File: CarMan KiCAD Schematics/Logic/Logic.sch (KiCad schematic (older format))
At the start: 33 parts, among them J1 MC_CAN, J3 IMU, J4 RTC, J5 Conn to TSI Board, J6 You're Welcome -Ethan, J7 RTC, J8 PIC program, U1 MCP9700AT-HTT, U3 PIC32MZ2048EFM064-I_PT, U5 ISO1050DUB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

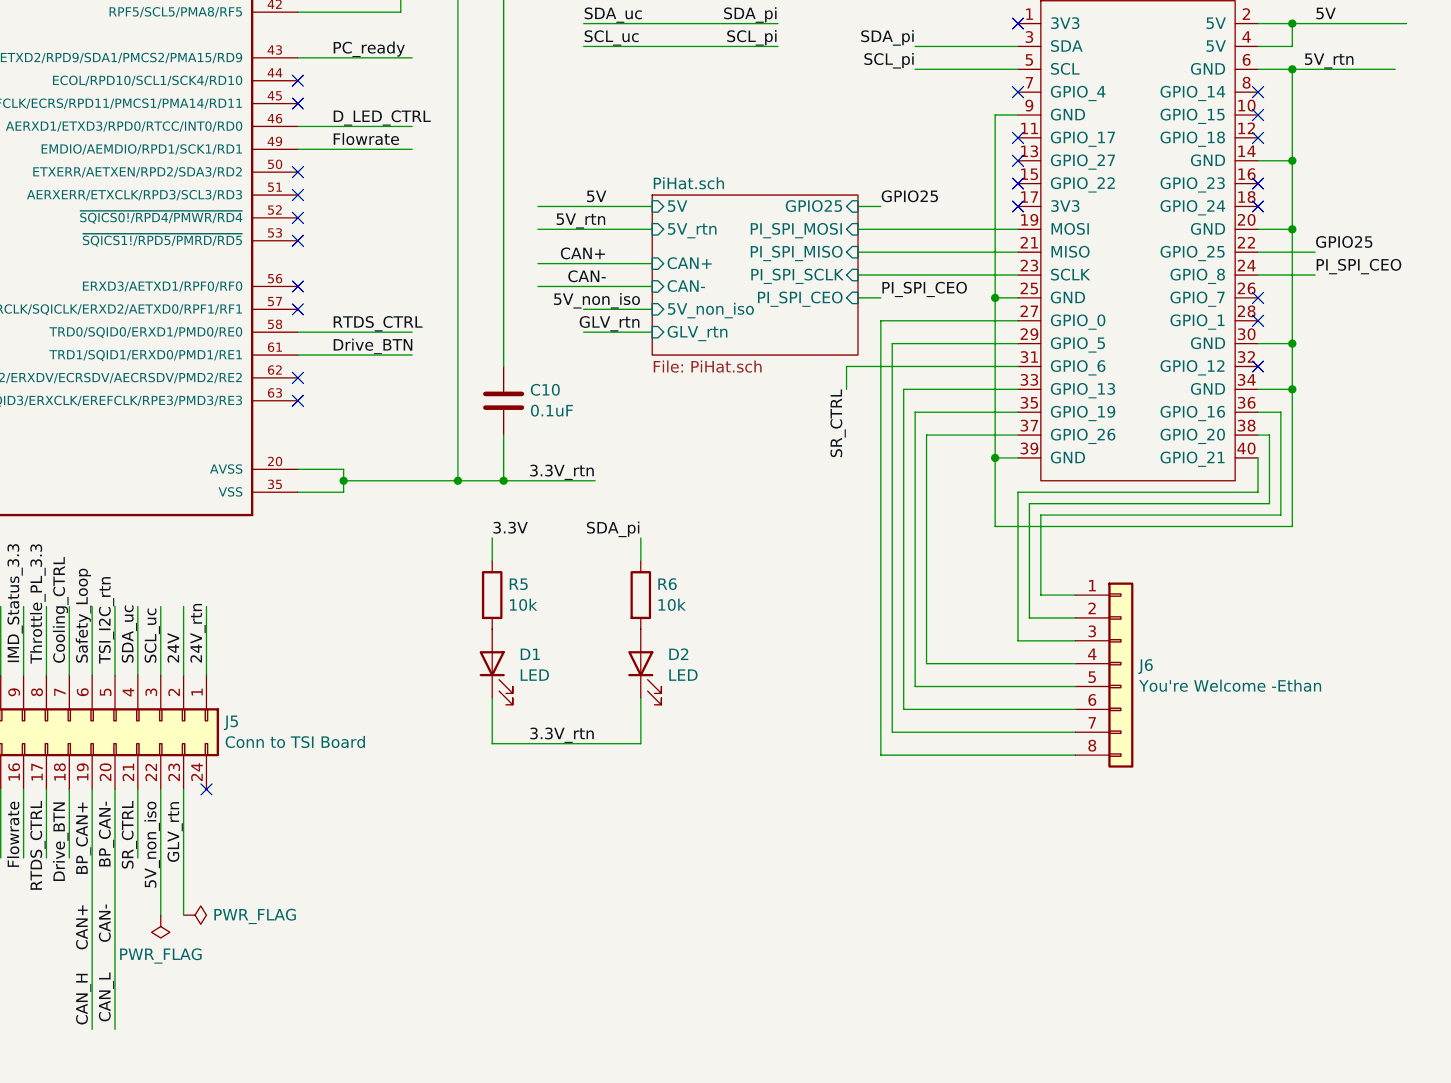
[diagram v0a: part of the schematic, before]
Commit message: Updated Pi GPIO and connector between Logic and TSI
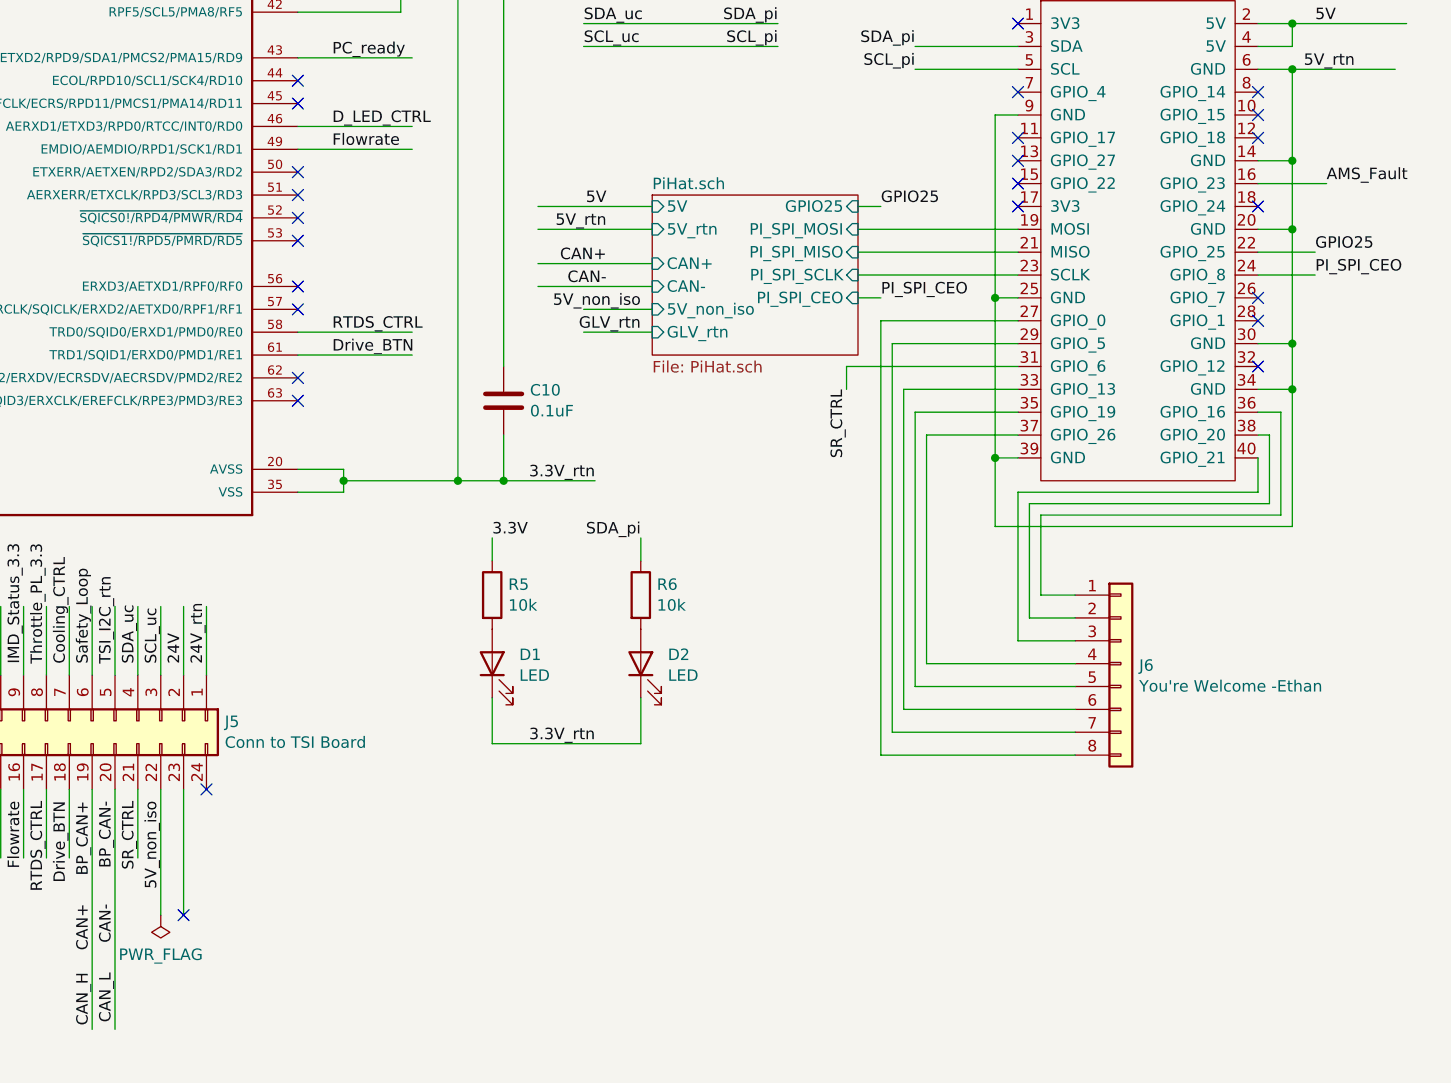
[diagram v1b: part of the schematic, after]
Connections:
- net labels added: AMS_Fault
- wire segments 247 -> 248
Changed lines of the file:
@@
 NoConn ~ 10550 4350
 NoConn ~ 10550 3950
-NoConn ~ 10550 3850
 NoConn ~ 10550 3650
 NoConn ~ 10550 3550
@@
 Wire Wire Line
 	5450 6500 5450 7550
-Text Label 5850 6550 3    50   ~ 0
-GLV_rtn
 Text Label 5750 6550 3    50   ~ 0
 5V_non_iso
@@
 	5850 6500 5850 7050
 $Comp
-L power:PWR_FLAG #FLG0105
-U 1 1 5FB4971B
-P 5850 7050
-F 0 "#FLG0105" H 5850 7125 50  0001 C CNN
-F 1 "PWR_FLAG" V 5850 7178 50  0000 L CNN
-F 2 "" H 5850 7050 50  0001 C CNN
-F 3 "~" H 5850 7050 50  0001 C CNN
-	1    5850 7050
-	0    1    1    0
-$EndComp
-$Comp
 L power:PWR_FLAG #FLG0106
 U 1 1 5FB4B178
@@
 Wire Wire Line
 	9550 2650 10000 2650
+NoConn ~ 5850 7050
+Wire Wire Line
+	10550 3850 10850 3850
+Text Label 10850 3850 0    50   ~ 0
+AMS_Fault
 $EndSCHEMATC

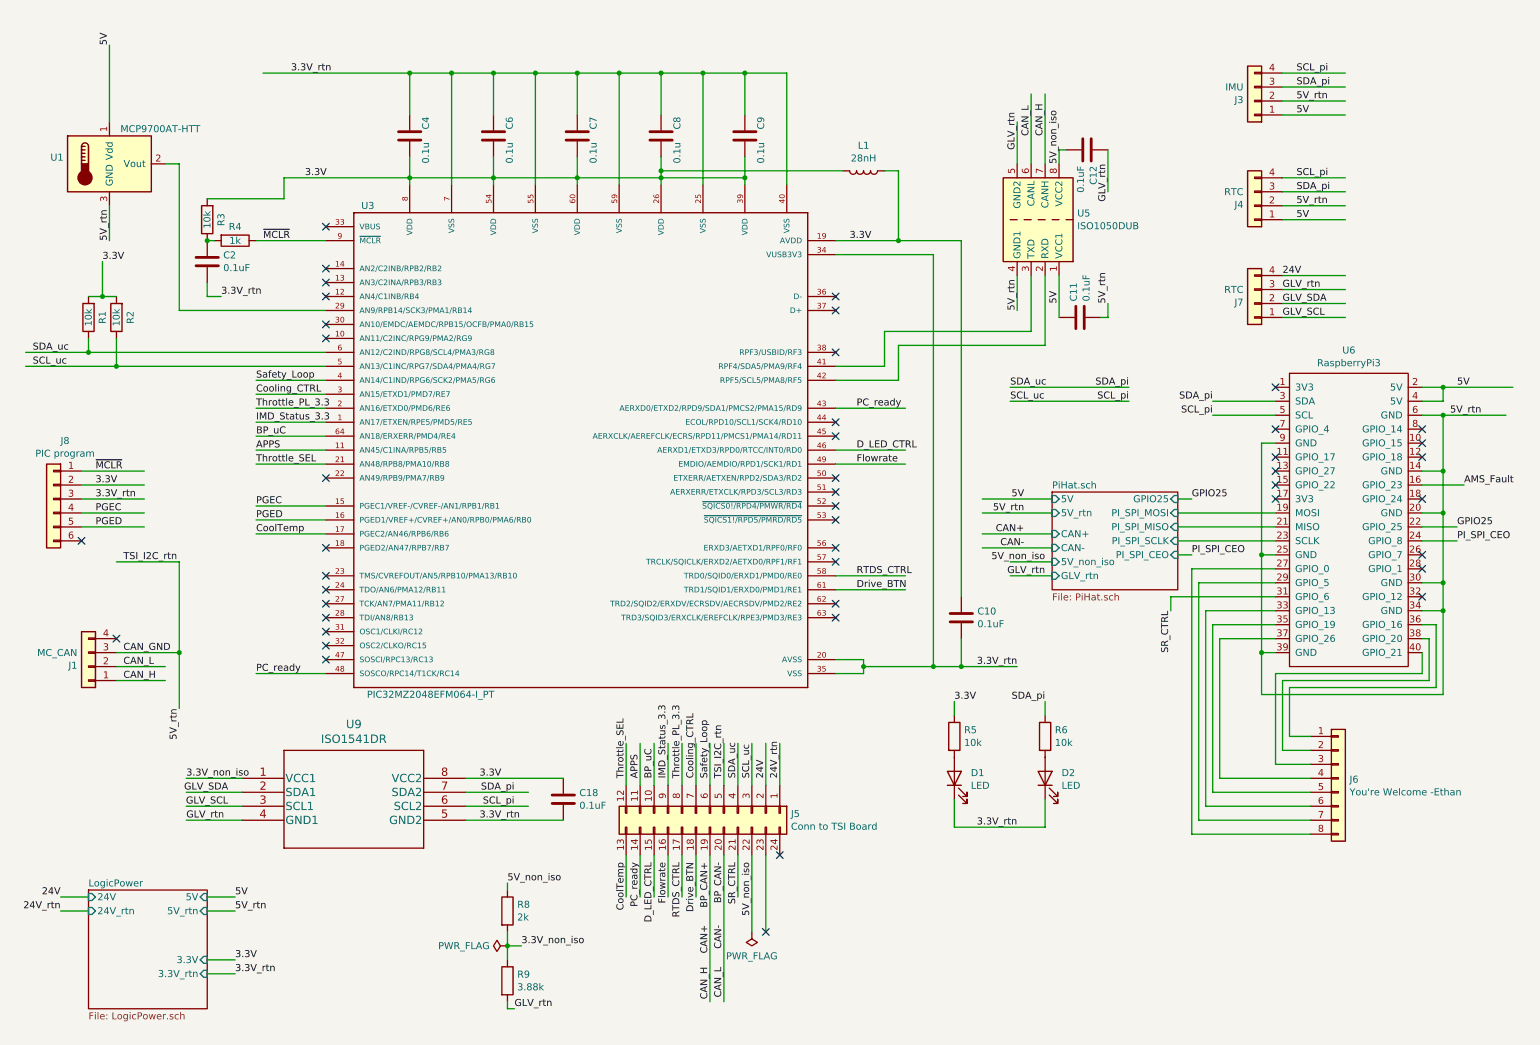
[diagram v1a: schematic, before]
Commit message: TSI: Added 24 to 12V converter, V dividers for IMD_Status, Throttle_PL, corrected pins 1-5 TSI-Logic Logic:24 to 5V non iso conv, safety_loop isolated, fixed I2C
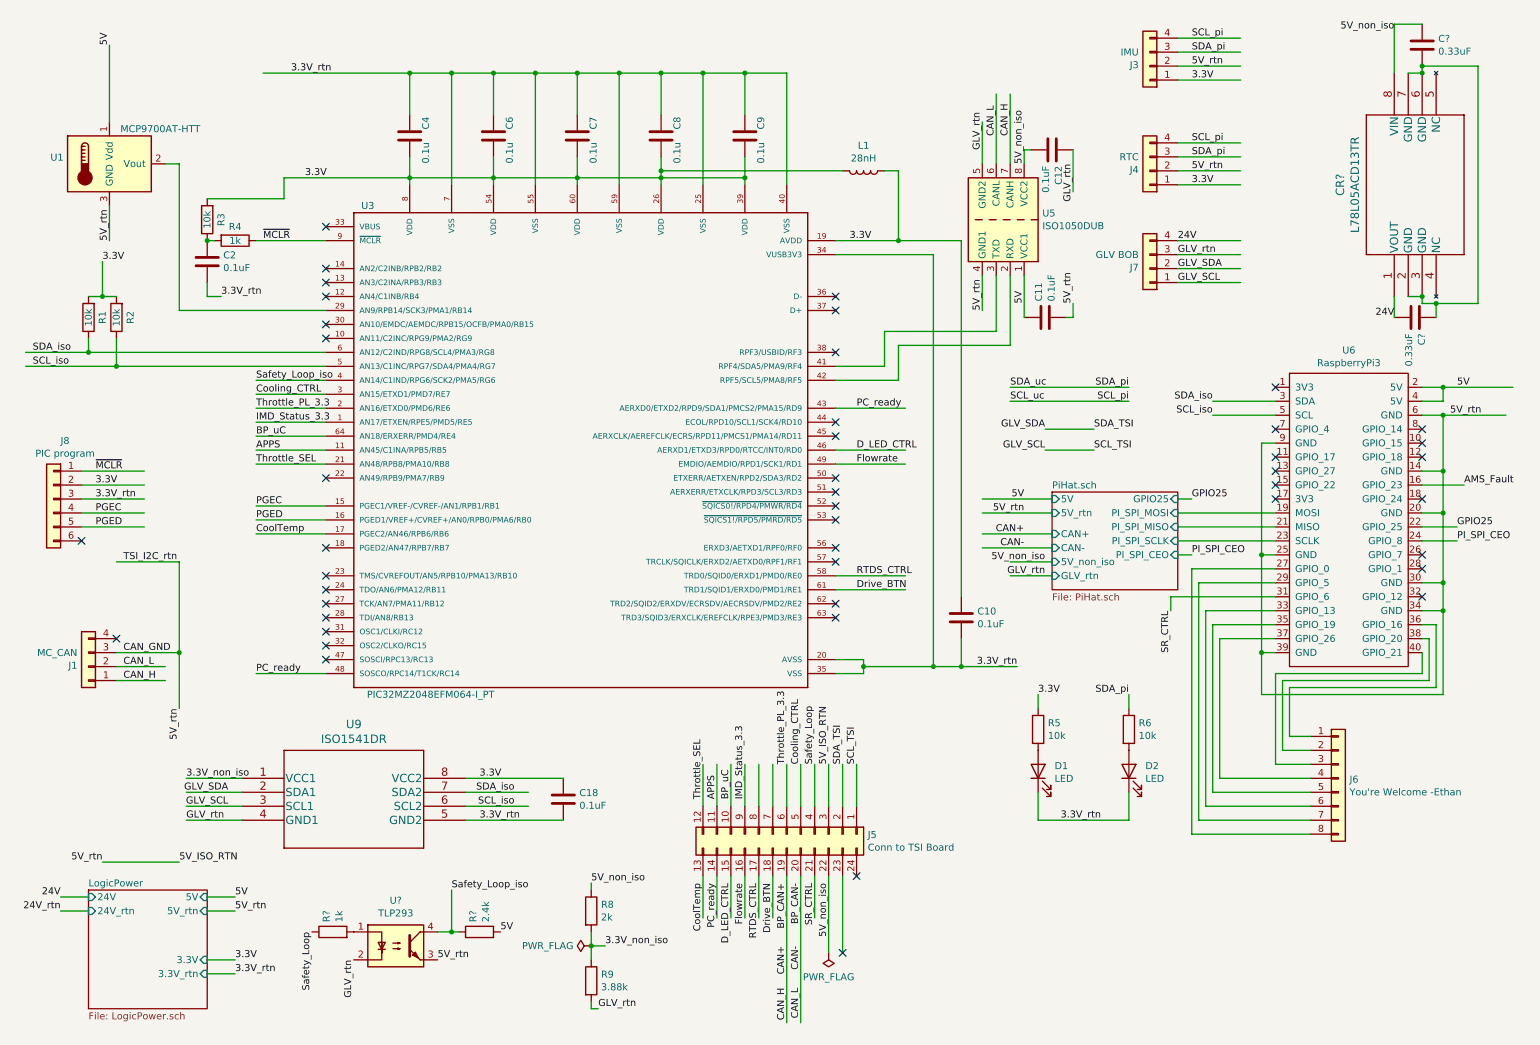
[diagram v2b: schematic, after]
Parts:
- added C? (x2): 0.33uF, symbol Device:C
- added CR?: L78L05ACD13TR, SO-8_STM, symbol CarMan_KiCAD_Library:L78L05ACD13TR
- added R?: 2.4k, symbol Device:R
- added R?: 1k, symbol Device:R
- added U?: TLP293, Package_SO:SOIC-4_4.55x2.6mm_P1.27mm, symbol CarMan_KiCAD_Library:TLP293
- J7: value RTC -> GLV BOB
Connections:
- net labels added: 5V_ISO_RTN, SCL_TSI, SCL_iso, SDA_TSI, SDA_iso, Safety_Loop_iso
- wire segments 248 -> 266
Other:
- moved on the sheet: C11, C12, D1, D2, J3, J4, J5, J7, R5, R6, R8, R9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

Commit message: fixed some bullshit
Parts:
- removed J5: Conn to TSI Board, symbol Logic-rescue:Conn_02x12_Counter_Clockwise-Connector_Generic-Logic-rescue
- added J5.1, J5.2: Conn_01x08, symbol Connector_Generic:Conn_01x08
- gave numbers to parts that had none: 6
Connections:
- net labels removed: APPS, BP_uC, CoolTemp, D_LED_CTRL, Drive_BTN, Flowrate, IMD_Status_3.3, Throttle_PL_3.3
- wire segments 266 -> 250
- no-connect marks 45 -> 53
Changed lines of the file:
@@
 Text Label 2200 3700 0    50   ~ 0
 Throttle_SEL
-Text Label 2200 3600 0    50   ~ 0
-APPS
 NoConn ~ 2700 2800
 NoConn ~ 2700 2700
@@
 NoConn ~ 2700 4300
 NoConn ~ 2700 3800
-Text Label 2200 3500 0    50   ~ 0
-BP_uC
-Text Label 2200 3400 0    50   ~ 0
-IMD_Status_3.3
-Text Label 2200 3300 0    50   ~ 0
-Throttle_PL_3.3
 Text Label 2200 3200 0    50   ~ 0
 Cooling_CTRL
@@
 Wire Wire Line
 	2700 3700 2200 3700
-Wire Wire Line
-	2700 3600 2200 3600
-Wire Wire Line
-	2700 3500 2200 3500
-Wire Wire Line
-	2700 3400 2200 3400
-Wire Wire Line
-	2700 3300 2200 3300
 Wire Wire Line
 	2700 3200 2200 3200
@@
 Wire Wire Line
 	2700 4000 2200 4000
-Text Label 2200 4200 0    50   ~ 0
-CoolTemp
-Wire Wire Line
-	2700 4200 2200 4200
 Text Label 6500 4500 0    50   ~ 0
 RTDS_CTRL
-Text Label 6500 4600 0    50   ~ 0
-Drive_BTN
 Text Label 6500 3300 0    50   ~ 0
 PC_ready
@@
 Wire Wire Line
 	2700 5200 2200 5200
-Text Label 6500 3700 0    50   ~ 0
-Flowrate
 Wire Wire Line
 	6800 2100 7250 2100
@@
 Text Label 1050 4150 0    50   ~ 0
 PGED
-Text Label 6500 3600 0    50   ~ 0
-D_LED_CTRL
 Wire Wire Line
 	8750 4650 8750 4750
@@
 Text Label 7850 4500 2    50   ~ 0
 GLV_rtn
-Text Label 6000 7450 3    50   ~ 0
+Text Label 6000 7500 3    50   ~ 0
 CAN_H
-Text Label 6100 7450 3    50   ~ 0
+Text Label 6100 7500 3    50   ~ 0
 CAN_L
 $Comp
@@
 Wire Wire Line
 	7400 1550 7400 1250
-Text Label 5500 6700 3    50   ~ 0
+Text Label 5900 6100 1    50   ~ 0
 PC_ready
-Text Label 5400 6700 3    50   ~ 0
-CoolTemp
-Text Label 5400 6100 1    50   ~ 0
+Text Label 6000 6100 1    50   ~ 0
 Throttle_SEL
-Text Label 5500 6100 1    50   ~ 0
-APPS
-Wire Wire Line
-	5500 5850 5500 6150
-Wire Wire Line
-	5400 5850 5400 6150
-Wire Wire Line
-	5400 6950 5400 6650
-Wire Wire Line
-	5500 6950 5500 6650
+Wire Wire Line
+	6000 5850 6000 6150
+Wire Wire Line
+	5900 5850 5900 6150
 Wire Wire Line
 	6550 5200 6350 5200
@@
 	6350 5100 6550 5100
 Wire Wire Line
-	6350 4600 6850 4600
-Wire Wire Line
 	6350 4500 6850 4500
-Wire Wire Line
-	6350 3700 6850 3700
-Wire Wire Line
-	6350 3600 6850 3600
 Wire Wire Line
 	6350 3300 6850 3300
@@
 $EndComp
 $Comp
-L CarMan_KiCAD_Library:TLP293 U?
+L CarMan_KiCAD_Library:TLP293 U10
 U 1 1 5FBF77BA
 P 3200 7150
-F 0 "U?" H 3200 7475 50  0000 C CNN
+F 0 "U10" H 3200 7475 50  0000 C CNN
 F 1 "TLP293" H 3200 7384 50  0000 C CNN
 F 2 "Package_SO:SOIC-4_4.55x2.6mm_P1.27mm" H 3000 6950 50  0001 L CIN
@@
 5V_rtn
 $Comp
-L Device:R R?
+L Device:R R12
 U 1 1 5FC0CCAA
 P 3800 7050
-F 0 "R?" H 3870 7096 50  0000 L CNN
+F 0 "R12" H 3870 7096 50  0000 L CNN
 F 1 "2.4k" H 3870 7005 50  0000 L CNN
 F 2 "" V 3730 7050 50  0001 C CNN
@@
 Safety_Loop_iso
 $Comp
-L Device:R R?
+L Device:R R11
 U 1 1 5FC4741F
 P 2750 7050
-F 0 "R?" H 2820 7096 50  0000 L CNN
+F 0 "R11" H 2820 7096 50  0000 L CNN
 F 1 "1k" H 2820 7005 50  0000 L CNN
 F 2 "" V 2680 7050 50  0001 C CNN
@@
 GLV_rtn
 $Comp
-L CarMan_KiCAD_Library:L78L05ACD13TR CR?
+L CarMan_KiCAD_Library:L78L05ACD13TR CR1
 U 1 1 5FC9A541
 P 10350 2500
-F 0 "CR?" H 11150 2887 60  0000 C CNN
+F 0 "CR1" H 11150 2887 60  0000 C CNN
 F 1 "L78L05ACD13TR" H 11150 2781 60  0000 C CNN
 F 2 "SO-8_STM" H 11150 2740 60  0001 C CNN
@@
 P 10500 2650
 AR Path="/5F9A7CF0/5FCEF62E" Ref="C?"  Part="1"
-AR Path="/5FCEF62E" Ref="C?"  Part="1"
-F 0 "C?" H 10615 2696 50  0000 L CNN
+AR Path="/5FCEF62E" Ref="C19"  Part="1"
+F 0 "C19" H 10615 2696 50  0000 L CNN
 F 1 "0.33uF" H 10615 2605 50  0000 L CNN
 F 2 "" H 10538 2500 50  0001 C CNN
@@
 P 10550 700
 AR Path="/5F9A7CF0/5FD53F31" Ref="C?"  Part="1"
-AR Path="/5FD53F31" Ref="C?"  Part="1"
-F 0 "C?" H 10665 746 50  0000 L CNN
+AR Path="/5FD53F31" Ref="C20"  Part="1"
+F 0 "C20" H 10665 746 50  0000 L CNN
 F 1 "0.33uF" H 10665 655 50  0000 L CNN
 F 2 "" H 10588 550 50  0001 C CNN
@@
 	1    0    0    -1
 $EndComp
-Wire Wire Line
-	10550 900  10450 900
 Text Label 10350 600  2    50   ~ 0
 5V_non_iso
@@
 	10550 850  10550 900
 Connection ~ 10550 850
-Connection ~ 10550 900
 Wire Wire Line
 	10550 550  10350 550
@@
 Text Label 6500 5850 1    50   ~ 0
 SCL_TSI
-NoConn ~ 6400 7200
 $Comp
 L power:PWR_FLAG #FLG0106
 U 1 1 5FB4B178
-P 6300 7200
-F 0 "#FLG0106" H 6300 7275 50  0001 C CNN
-F 1 "PWR_FLAG" H 6300 7373 50  0000 C CNN
-F 2 "" H 6300 7200 50  0001 C CNN
-F 3 "~" H 6300 7200 50  0001 C CNN
-	1    6300 7200
+P 6300 7250
+F 0 "#FLG0106" H 6300 7325 50  0001 C CNN
+F 1 "PWR_FLAG" H 6300 7423 50  0000 C CNN
+F 2 "" H 6300 7250 50  0001 C CNN
+F 3 "~" H 6300 7250 50  0001 C CNN
+	1    6300 7250
 	-1   0    0    1
 $EndComp
 Wire Wire Line
-	6400 6650 6400 7200
-Wire Wire Line
-	6300 6650 6300 7200
+	6300 6700 6300 7250
 Wire Wire Line
 	6500 6150 6500 5850
@@
 	6100 6150 6100 5850
 Wire Wire Line
-	6000 6150 6000 5850
-Wire Wire Line
-	5900 6150 5900 5850
-Wire Wire Line
-	5800 6150 5800 5850
-Wire Wire Line
-	5700 6150 5700 5850
-Wire Wire Line
-	5600 6150 5600 5850
-Wire Wire Line
-	5900 6950 5900 6650
-Wire Wire Line
-	5800 6950 5800 6650
-Wire Wire Line
-	5700 6950 5700 6650
-Wire Wire Line
-	5600 6950 5600 6650
+	5900 7000 5900 6700
 Text Label 6400 5850 1    50   ~ 0
 SDA_TSI
 Text Label 6100 5850 1    50   ~ 0
 Cooling_CTRL
-Text Label 6000 5850 1    50   ~ 0
-Throttle_PL_3.3
-Text Label 5700 6100 1    50   ~ 0
-IMD_Status_3.3
-Text Label 5600 6100 1    50   ~ 0
-BP_uC
-Text Label 5700 6700 3    50   ~ 0
-Flowrate
-Text Label 5800 6700 3    50   ~ 0
+Text Label 5900 6750 3    50   ~ 0
 RTDS_CTRL
-Text Label 5900 6700 3    50   ~ 0
-Drive_BTN
-Text Label 6000 6700 3    50   ~ 0
+Text Label 6000 7200 3    50   ~ 0
+CAN+
+Text Label 6100 7200 3    50   ~ 0
+CAN-
+Wire Wire Line
+	6200 6700 6200 7000
+Text Label 6200 6750 3    50   ~ 0
+SR_CTRL
+Text Label 6300 6750 3    50   ~ 0
+5V_non_iso
+NoConn ~ 2700 3300
+NoConn ~ 5800 6150
+NoConn ~ 2700 3400
+NoConn ~ 2700 3500
+NoConn ~ 2700 3600
+NoConn ~ 2700 4200
+NoConn ~ 6350 4600
+NoConn ~ 6350 3600
+NoConn ~ 6350 3700
+$Comp
+L Connector_Generic:Conn_01x08 J5.1
+U 1 1 5FCBCDE5
+P 6200 6350
+F 0 "J5.1" V 6118 6730 50  0000 L CNN
+F 1 "Conn_01x08" V 6163 6730 50  0001 L CNN
+F 2 "" H 6200 6350 50  0001 C CNN
+F 3 "~" H 6200 6350 50  0001 C CNN
+	1    6200 6350
+	0    1    1    0
+$EndComp
+$Comp
+L Connector_Generic:Conn_01x08 J5.2
+U 1 1 5FCE2C74
+P 6200 6500
+F 0 "J5.2" V 6118 6880 50  0000 L CNN
+F 1 "Conn_01x08" V 6163 6880 50  0001 L CNN
+F 2 "" H 6200 6500 50  0001 C CNN
+F 3 "~" H 6200 6500 50  0001 C CNN
+	1    6200 6500
+	0    1    -1   0
+$EndComp
+NoConn ~ 5800 6700
+Wire Wire Line
+	6100 6700 6100 7750
+Wire Wire Line
+	6000 6700 6000 7750
+Text Label 6100 6750 3    50   ~ 0
+BP_CAN-
+Text Label 6000 6750 3    50   ~ 0
 BP_CAN+
-Text Label 6100 6700 3    50   ~ 0
-BP_CAN-
-Text Label 6000 7150 3    50   ~ 0
-CAN+
-Text Label 6100 7150 3    50   ~ 0
-CAN-
-Text Label 5600 6700 3    50   ~ 0
-D_LED_CTRL
-$Comp
-L Logic-rescue:Conn_02x12_Counter_Clockwise-Connector_Generic-Logic-rescue J5
-U 1 1 5F9DBA92
-P 6000 6350
-F 0 "J5" V 6004 6930 50  0000 L CNN
-F 1 "Conn to TSI Board" V 6095 6930 50  0000 L CNN
-F 2 "" H 6000 6350 50  0001 C CNN
-F 3 "~" H 6000 6350 50  0001 C CNN
-	1    6000 6350
-	0    1    1    0
-$EndComp
-Wire Wire Line
-	6200 6650 6200 6950
-NoConn ~ 6500 6650
-Text Label 6200 6700 3    50   ~ 0
-SR_CTRL
-Text Label 6300 6700 3    50   ~ 0
-5V_non_iso
-Wire Wire Line
-	6000 6650 6000 7700
-Wire Wire Line
-	6100 6650 6100 7700
+Wire Wire Line
+	6500 6700 6500 7000
+Wire Wire Line
+	6400 6700 6400 7000
+Text Label 6500 7000 3    50   ~ 0
+AMS_Fault
+Text Label 6400 7000 3    50   ~ 0
+GLV_rtn
+Text Label 10950 1700 0    50   ~ 0
+GLV_rtn
+Wire Wire Line
+	10550 850  10450 850
+Wire Wire Line
+	10450 850  10450 900
 $EndSCHEMATC
